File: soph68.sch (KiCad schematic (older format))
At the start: 235 parts, among them J1 STLINK_6_Pin, U1 SRV05-4, U2 STM32F072C8Tx, U3 AMS1117-5.0

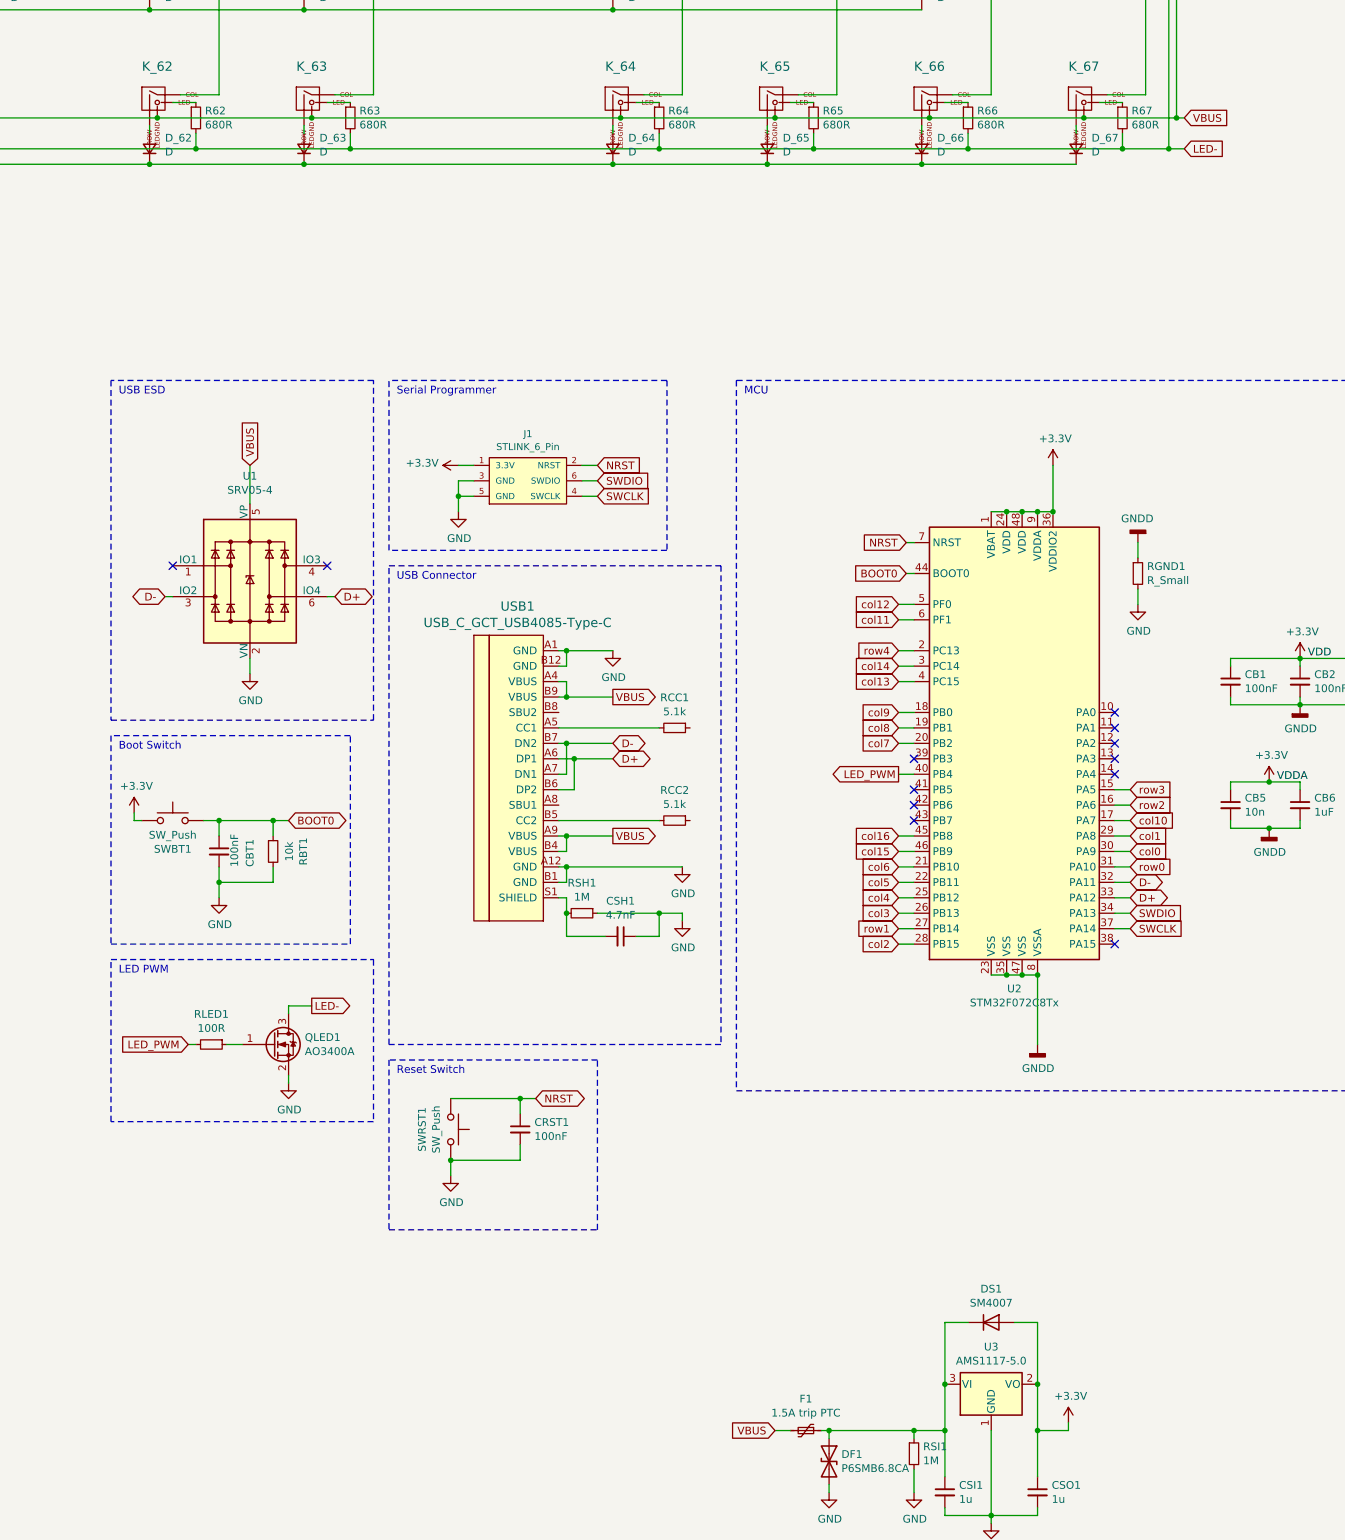
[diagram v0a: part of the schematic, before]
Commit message: fixing some schema troubles
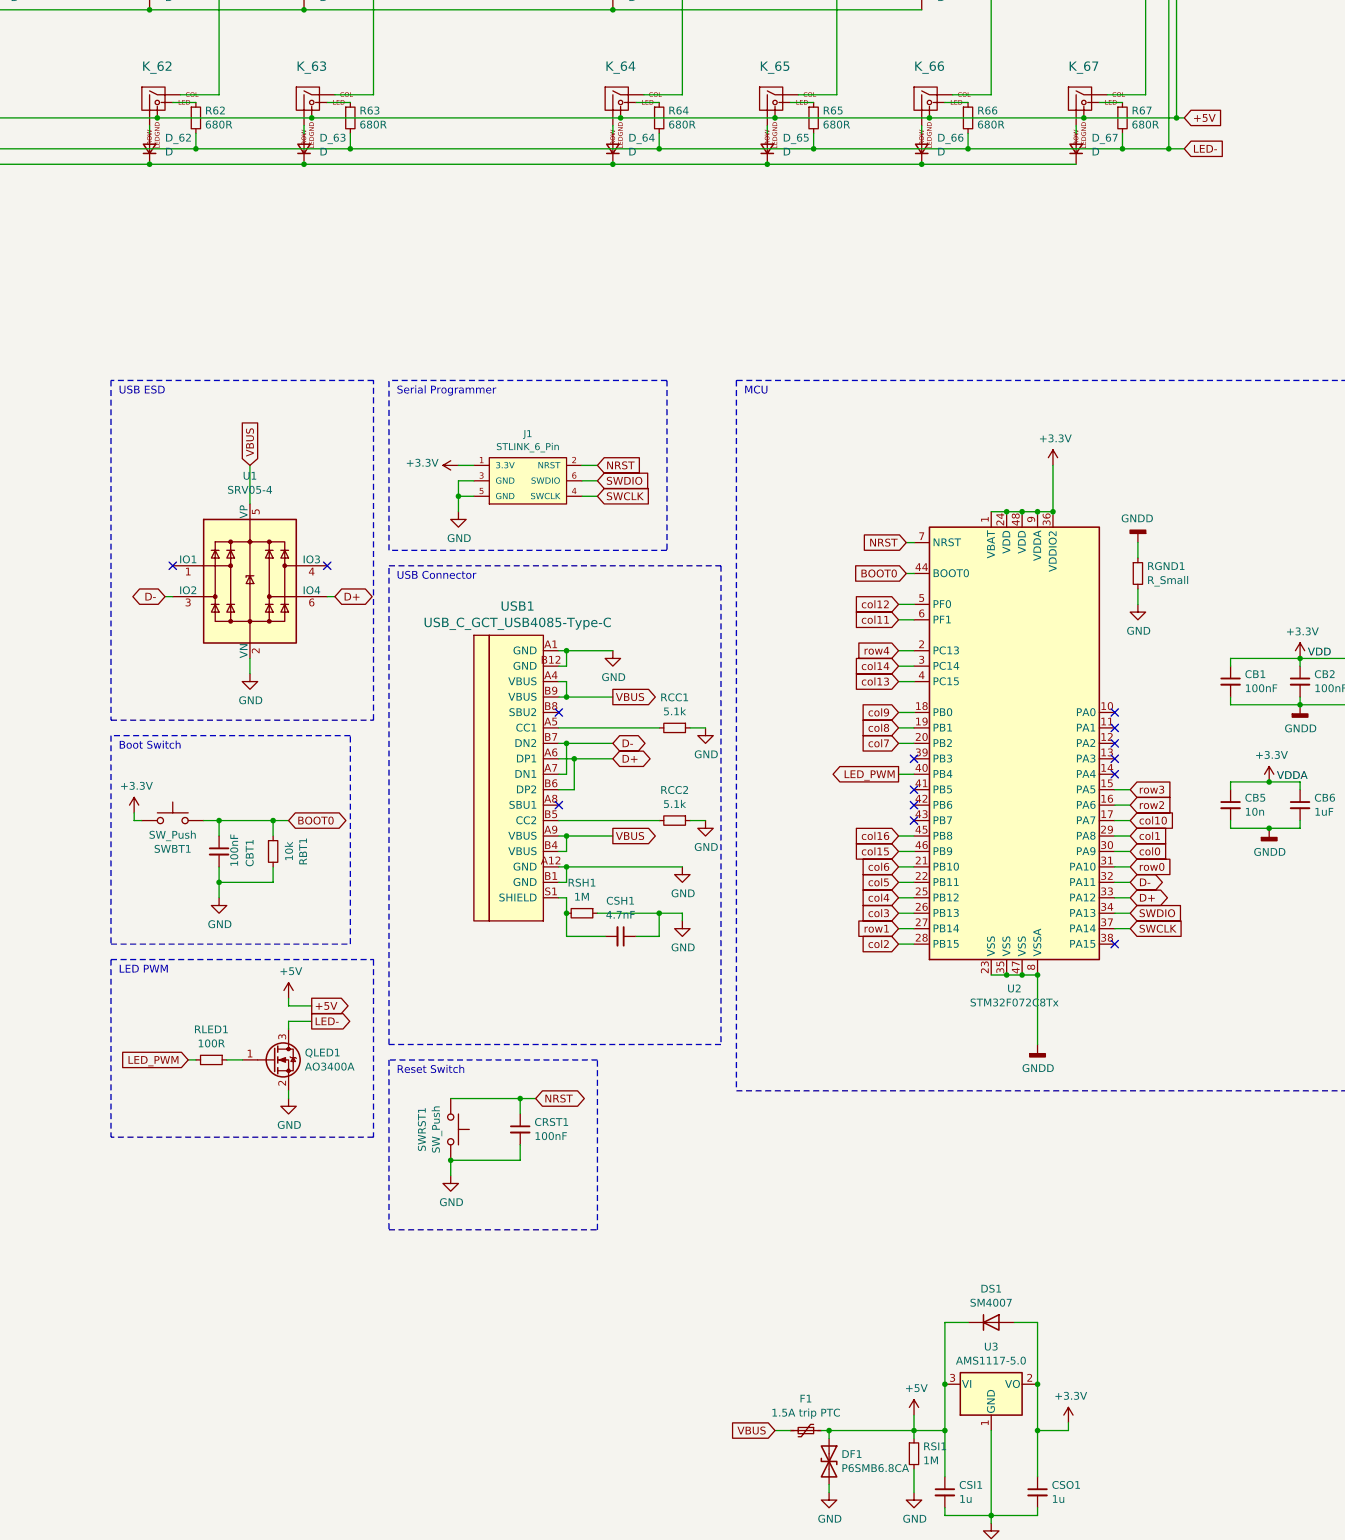
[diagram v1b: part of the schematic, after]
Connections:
- net GND: now also RCC1.1, RCC2.1
- net VBUS: no longer K_0.4 (LEDGND), K_1.4 (LEDGND), K_10.4 (LEDGND), K_11.4 (LEDGND), K_12.4 (LEDGND), K_13.4 (LEDGND), K_14.4 (LEDGND), K_15.4 (LEDGND), K_16.4 (LEDGND), K_17.4 (LEDGND), K_18.4 (LEDGND), K_19.4 (LEDGND), K_2.4 (LEDGND), K_20.4 (LEDGND), K_21.4 (LEDGND), K_22.4 (LEDGND), K_23.4 (LEDGND), K_24.4 (LEDGND), K_25.4 (LEDGND), K_26.4 (LEDGND), K_27.4 (LEDGND), K_28.4 (LEDGND), K_29.4 (LEDGND), K_3.4 (LEDGND), K_30.4 (LEDGND), K_31.4 (LEDGND), K_32.4 (LEDGND), K_33.4 (LEDGND), K_34.4 (LEDGND), K_35.4 (LEDGND), K_36.4 (LEDGND), K_37.4 (LEDGND), K_38.4 (LEDGND), K_39.4 (LEDGND), K_4.4 (LEDGND), K_40.4 (LEDGND), K_41.4 (LEDGND), K_42.4 (LEDGND), K_43.4 (LEDGND), K_44.4 (LEDGND), K_45.4 (LEDGND), K_46.4 (LEDGND), K_47.4 (LEDGND), K_48.4 (LEDGND), K_49.4 (LEDGND), K_5.4 (LEDGND), K_50.4 (LEDGND), K_51.4 (LEDGND), K_52.4 (LEDGND), K_53.4 (LEDGND), K_54.4 (LEDGND), K_55.4 (LEDGND), K_56.4 (LEDGND), K_57.4 (LEDGND), K_58.4 (LEDGND), K_59.4 (LEDGND), K_6.4 (LEDGND), K_60.4 (LEDGND), K_61.4 (LEDGND), K_62.4 (LEDGND), K_63.4 (LEDGND), K_64.4 (LEDGND), K_65.4 (LEDGND), K_66.4 (LEDGND), K_67.4 (LEDGND), K_7.4 (LEDGND), K_8.4 (LEDGND), K_9.4 (LEDGND)
- net +5V: now reaches CSI1.1, DF1.1 (A1), DS1.1 (K), F1.1, RSI1.1, U3.3 (VI)
- net +5V: now also K_0.4 (LEDGND), K_1.4 (LEDGND), K_10.4 (LEDGND), K_11.4 (LEDGND), K_12.4 (LEDGND), K_13.4 (LEDGND), K_14.4 (LEDGND), K_15.4 (LEDGND), K_16.4 (LEDGND), K_17.4 (LEDGND), K_18.4 (LEDGND), K_19.4 (LEDGND), K_2.4 (LEDGND), K_20.4 (LEDGND), K_21.4 (LEDGND), K_22.4 (LEDGND), K_23.4 (LEDGND), K_24.4 (LEDGND), K_25.4 (LEDGND), K_26.4 (LEDGND), K_27.4 (LEDGND), K_28.4 (LEDGND), K_29.4 (LEDGND), K_3.4 (LEDGND), K_30.4 (LEDGND), K_31.4 (LEDGND), K_32.4 (LEDGND), K_33.4 (LEDGND), K_34.4 (LEDGND), K_35.4 (LEDGND), K_36.4 (LEDGND), K_37.4 (LEDGND), K_38.4 (LEDGND), K_39.4 (LEDGND), K_4.4 (LEDGND), K_40.4 (LEDGND), K_41.4 (LEDGND), K_42.4 (LEDGND), K_43.4 (LEDGND), K_44.4 (LEDGND), K_45.4 (LEDGND), K_46.4 (LEDGND), K_47.4 (LEDGND), K_48.4 (LEDGND), K_49.4 (LEDGND), K_5.4 (LEDGND), K_50.4 (LEDGND), K_51.4 (LEDGND), K_52.4 (LEDGND), K_53.4 (LEDGND), K_54.4 (LEDGND), K_55.4 (LEDGND), K_56.4 (LEDGND), K_57.4 (LEDGND), K_58.4 (LEDGND), K_59.4 (LEDGND), K_6.4 (LEDGND), K_60.4 (LEDGND), K_61.4 (LEDGND), K_62.4 (LEDGND), K_63.4 (LEDGND), K_64.4 (LEDGND), K_65.4 (LEDGND), K_66.4 (LEDGND), K_67.4 (LEDGND), K_7.4 (LEDGND), K_8.4 (LEDGND), K_9.4 (LEDGND)
- no-connect marks 12 -> 14
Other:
- moved on the sheet: QLED1, RLED1
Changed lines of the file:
@@
 EESchema Schematic File Version 4
+LIBS:soph68-cache
 EELAYER 30 0
 EELAYER END
@@
 Connection ~ 18000 5100
 Text GLabel 18050 5100 2    50   Input ~ 0
-VBUS
++5V
 Text GLabel 18050 5300 2    50   Input ~ 0
 LED-
@@
 L Device:R_Small RLED1
 U 1 1 6309702D
-P 11750 11100
-F 0 "RLED1" V 11554 11100 50  0000 C CNN
-F 1 "100R" V 11645 11100 50  0000 C CNN
-F 2 "Resistor_SMD:R_0402_1005Metric" H 11750 11100 50  0001 C CNN
-F 3 "~" H 11750 11100 50  0001 C CNN
-F 4 "C25076" V 11750 11100 50  0001 C CNN "JLCCode"
-	1    11750 11100
+P 11750 11200
+F 0 "RLED1" V 11554 11200 50  0000 C CNN
+F 1 "100R" V 11645 11200 50  0000 C CNN
+F 2 "Resistor_SMD:R_0402_1005Metric" H 11750 11200 50  0001 C CNN
+F 3 "~" H 11750 11200 50  0001 C CNN
+F 4 "C25076" V 11750 11200 50  0001 C CNN "JLCCode"
+	1    11750 11200
 	0    1    1    0
 $EndComp
@@
 L Device:Q_NMOS_GSD QLED1
 U 1 1 63098D59
-P 12150 11100
-F 0 "QLED1" H 12355 11146 50  0000 L CNN
-F 1 "AO3400A" H 12355 11055 50  0000 L CNN
-F 2 "Package_TO_SOT_SMD:SOT-23" H 12350 11025 50  0001 L CIN
-F 3 "https://datasheet.lcsc.com/szlcsc/Alpha-Omega-Semicon-AOS-AO3400A_C20917.pdf" H 12150 11100 50  0001 L CNN
-F 4 "C20917" H 12150 11100 50  0001 C CNN "JLCCode"
-	1    12150 11100
+P 12150 11200
+F 0 "QLED1" H 12355 11246 50  0000 L CNN
+F 1 "AO3400A" H 12355 11155 50  0000 L CNN
+F 2 "Package_TO_SOT_SMD:SOT-23" H 12350 11125 50  0001 L CIN
+F 3 "https://datasheet.lcsc.com/szlcsc/Alpha-Omega-Semicon-AOS-AO3400A_C20917.pdf" H 12150 11200 50  0001 L CNN
+F 4 "C20917" H 12150 11200 50  0001 C CNN "JLCCode"
+	1    12150 11200
 	1    0    0    -1
 $EndComp
 Wire Wire Line
-	11950 11100 11850 11100
+	11950 11200 11850 11200
 Wire Wire Line
-	12250 10900 12250 10850
+	12250 11000 12250 10950
 Wire Wire Line
-	12250 10850 12400 10850
+	12250 10950 12400 10950
 Wire Wire Line
-	12250 11300 12250 11350
+	12250 11400 12250 11450
 $Comp
 L power:GND #PWR0121
 U 1 1 6320C39E
-P 12250 11350
-F 0 "#PWR0121" H 12250 11100 50  0001 C CNN
-F 1 "GND" H 12255 11177 50  0000 C CNN
-F 2 "" H 12250 11350 50  0001 C CNN
-F 3 "" H 12250 11350 50  0001 C CNN
-	1    12250 11350
+P 12250 11450
+F 0 "#PWR0121" H 12250 11200 50  0001 C CNN
+F 1 "GND" H 12255 11277 50  0000 C CNN
+F 2 "" H 12250 11450 50  0001 C CNN
+F 3 "" H 12250 11450 50  0001 C CNN
+	1    12250 11450
 	1    0    0    -1
 $EndComp
-Text GLabel 12400 10850 2    50   Output ~ 0
+Text GLabel 12400 10950 2    50   Output ~ 0
 LED-
-Text GLabel 11600 11100 0    50   Input ~ 0
+Text GLabel 11600 11200 0    50   Input ~ 0
 LED_PWM
 Wire Wire Line
-	11600 11100 11650 11100
-Wire Notes Line
-	12800 11600 11100 11600
+	11600 11200 11650 11200
 Wire Notes Line
-	11100 11600 11100 10550
+	12800 11700 11100 11700
 Wire Notes Line
 	11100 10550 12800 10550
-Wire Notes Line
-	12800 10550 12800 11600
 Text Notes 11150 10650 0    50   ~ 0
 LED PWM
@@
 Wire Wire Line
 	16800 14150 17100 14150
+$Comp
+L power:+5V #PWR0127
+U 1 1 5F197C04
+P 16300 13500
+F 0 "#PWR0127" H 16300 13350 50  0001 C CNN
+F 1 "+5V" H 16315 13673 50  0000 C CNN
+F 2 "" H 16300 13500 50  0001 C CNN
+F 3 "" H 16300 13500 50  0001 C CNN
+	1    16300 13500
+	1    0    0    -1
+$EndComp
+Wire Wire Line
+	16300 13500 16300 13600
+$Comp
+L power:+5V #PWR0128
+U 1 1 5F22B318
+P 12250 10800
+F 0 "#PWR0128" H 12250 10650 50  0001 C CNN
+F 1 "+5V" H 12265 10973 50  0000 C CNN
+F 2 "" H 12250 10800 50  0001 C CNN
+F 3 "" H 12250 10800 50  0001 C CNN
+	1    12250 10800
+	1    0    0    -1
+$EndComp
+Text GLabel 12400 10850 2    50   Output ~ 0
++5V
+Wire Notes Line
+	12800 10550 12800 11700
+Wire Notes Line
+	11100 10550 11100 11700
+Wire Wire Line
+	12250 10800 12250 10850
+Wire Wire Line
+	12250 10850 12400 10850
+NoConn ~ 14000 8950
+NoConn ~ 14000 9550
+$Comp
+L power:GND #PWR0129
+U 1 1 5F626B8A
+P 14950 9650
+F 0 "#PWR0129" H 14950 9400 50  0001 C CNN
+F 1 "GND" H 14955 9477 50  0000 C CNN
+F 2 "" H 14950 9650 50  0001 C CNN
+F 3 "" H 14950 9650 50  0001 C CNN
+	1    14950 9650
+	1    0    0    -1
+$EndComp
+$Comp
+L power:GND #PWR0130
+U 1 1 5F6270A7
+P 14950 9050
+F 0 "#PWR0130" H 14950 8800 50  0001 C CNN
+F 1 "GND" H 14955 8877 50  0000 C CNN
+F 2 "" H 14950 9050 50  0001 C CNN
+F 3 "" H 14950 9050 50  0001 C CNN
+	1    14950 9050
+	1    0    0    -1
+$EndComp
+Wire Wire Line
+	14950 9050 14850 9050
+Wire Wire Line
+	14850 9650 14950 9650
 $EndSCHEMATC
